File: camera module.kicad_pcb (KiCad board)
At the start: 2 copper layers, 11.4 x 5.7 mm, 152 parts, among them J1 Conn_01x02, J10 Conn_01x04, J11 Conn_01x05, J12 Conn_01x06, J13 Conn_01x02, J15 Conn_02x30_Odd_Even, J17 USB_B_Micro, J18 Conn_01x03, J2 USB_OTG, J3 Conn_01x15, J4 Conn_02x15_Counter_Clockwise, J5 HDMI, J6 Conn_01x15, J7 Conn_01x02, J8 HDMI, J9 HDMI, Q1 EM6K34T2CR, Q10 DMG2305UX, Q11 DMMT5401-7-F, Q12 DMG2305UX, Q2 Q_NMOS_GSD, Q3 Q_NMOS_GSD, Q4 Q_NMOS_GSD, Q5 Q_NMOS_GSD, Q6 Q_NMOS_GSD, Q7 DMMT5401-7-F, Q8 DMG2305UX, Q9 DMMT5401-7-F, SW1 SW_SPST, U1 TPS563208, U10 FSUSB42UMX, U11 USB_A, U2 PAM2306AYPKE, U3 LTC3406ES5-1.2, U4 TS3DDR3812RUAR, U5 TLV70228_SOT23-5, U6 XC6222B181MR-G, U7 LSM6DS3, U8 HDMIULC6-4SC6, U9 AP2331W, Y1 SIT8008AI-73-XXS-33.333333E

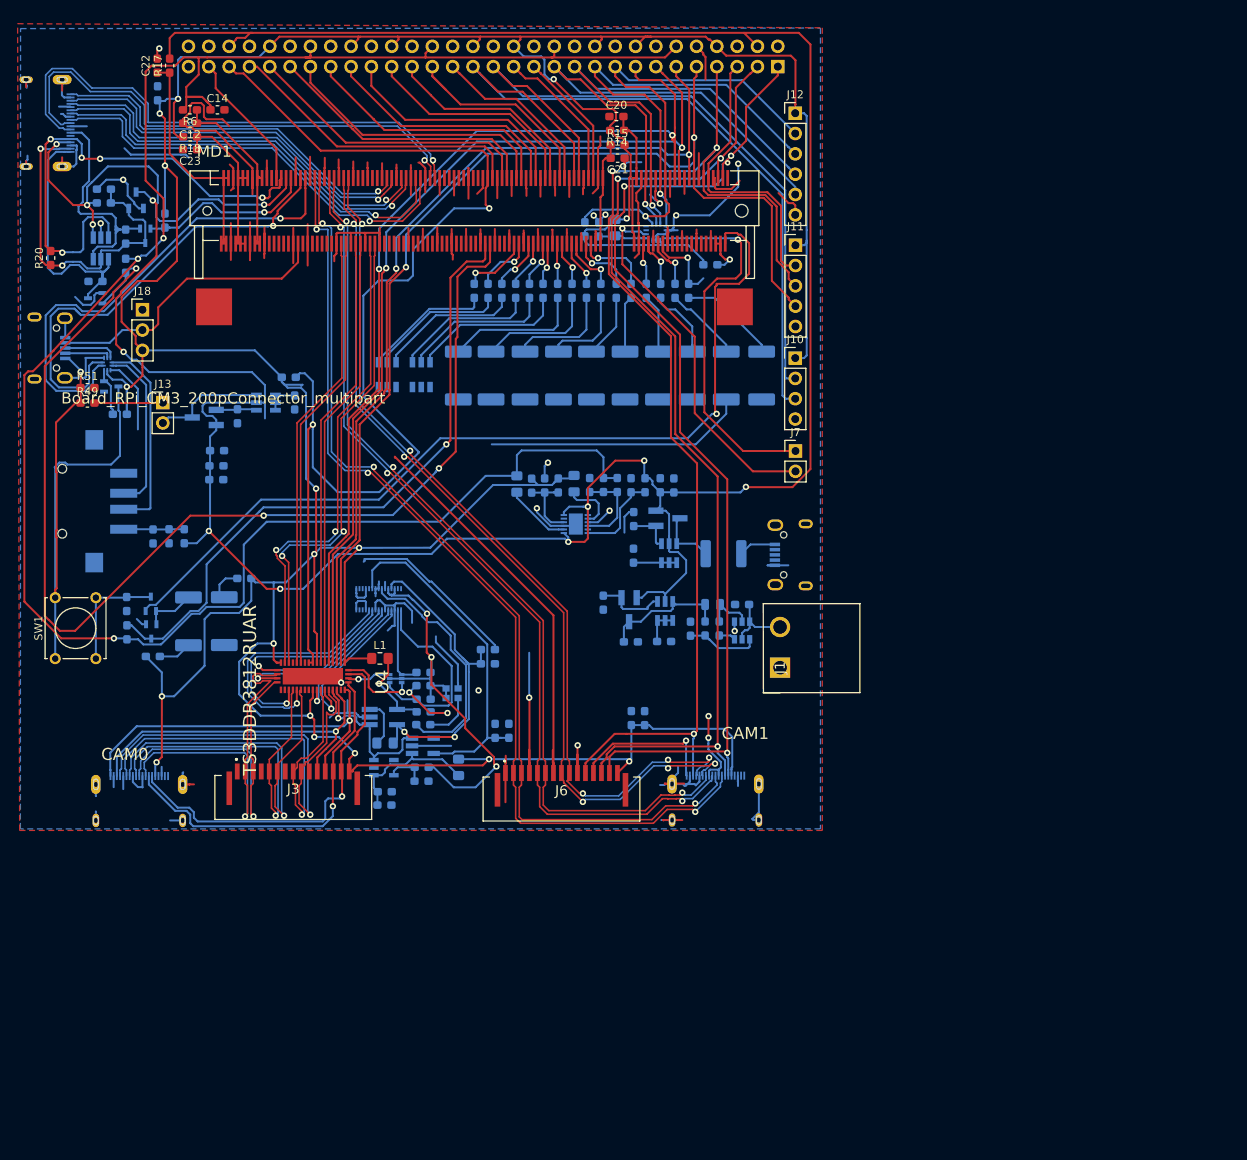
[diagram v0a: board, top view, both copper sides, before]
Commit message: Tweaks to routing, 4th mounting hole added, DRC issues fixed
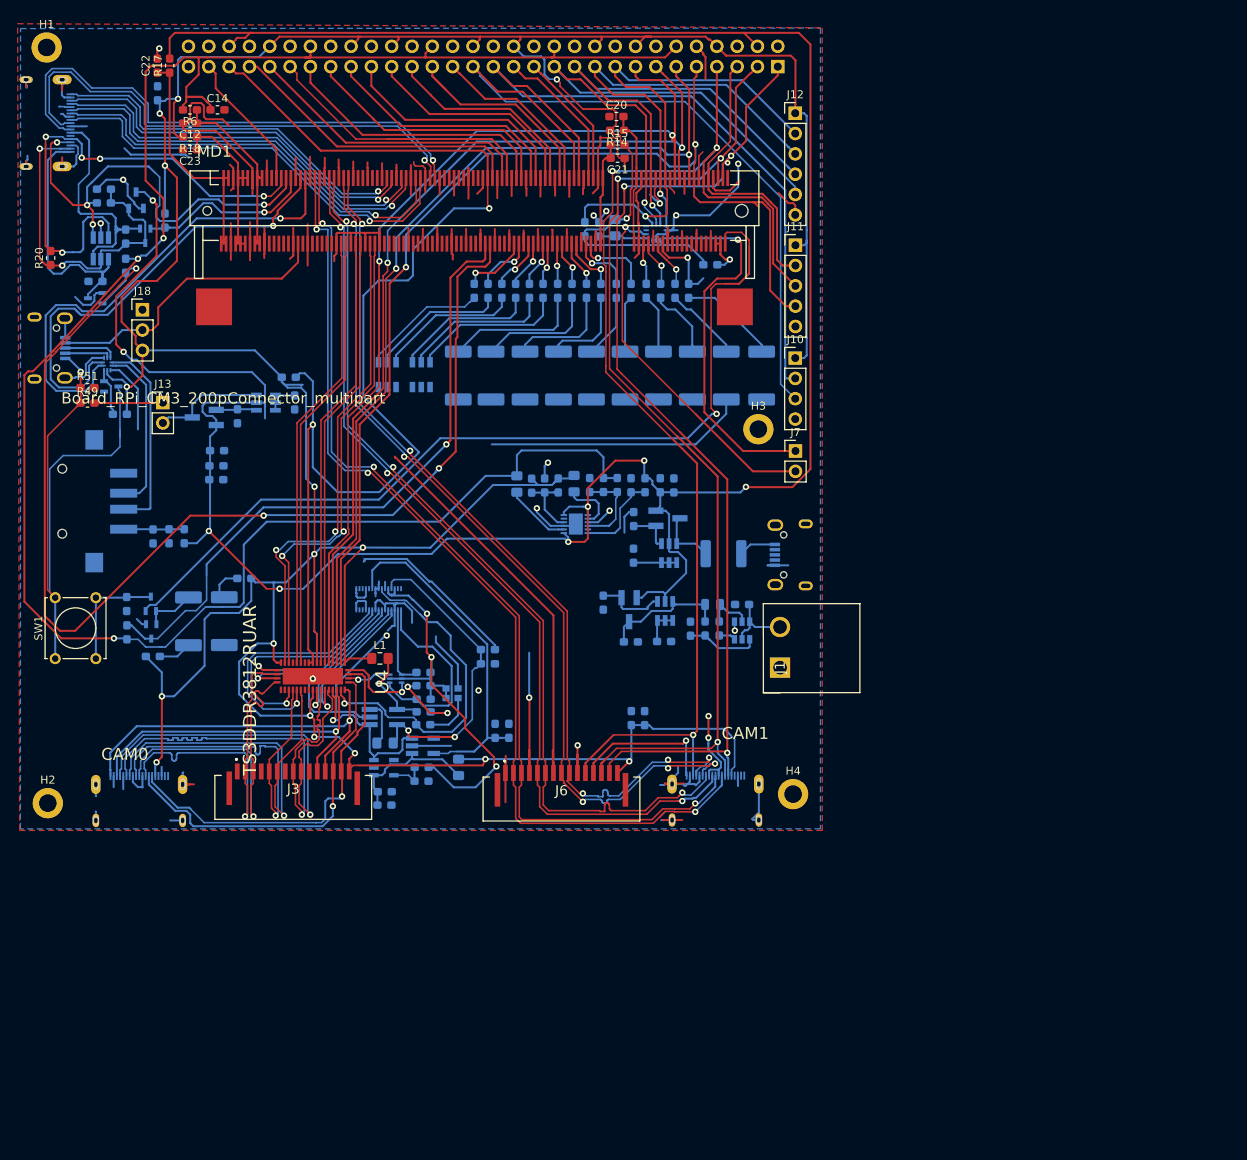
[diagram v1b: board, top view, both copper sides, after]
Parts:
- added H1: MountingHole, MountingHole:MountingHole_2.2mm_M2_DIN965_Pad, F.Cu at (50.9, 38.5)
- added H2: MountingHole, MountingHole:MountingHole_2.2mm_M2_DIN965_Pad, F.Cu at (51.0, 133.0)
- added H3: MountingHole, MountingHole:MountingHole_2.2mm_M2_DIN965_Pad, F.Cu at (139.8, 86.2)
- added H4: MountingHole, MountingHole:MountingHole_2.2mm_M2_DIN965_Pad, F.Cu at (144.2, 131.9)
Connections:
- J4 pad 24: CAM0_CLK -> CAM0_onboard_CLK
- R13 pad 1: CAM0_CLK -> CAM0_onboard_CLK
- U4 pad 37: CAM0_onboard_CK -> CAM0_onboard_CLK
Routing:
- net CAM0_onboard_CLK: track 0.00 -> 44.7 mm, vias 0 -> 1
- net CAM0_CLK: track 29.8 -> 0.00 mm
- net GND: track 567.6 -> 585.4 mm
- net CAM0_offboard_CN: track 53.3 -> 56.5 mm
- net CAM0_offboard_DP0: track 43.2 -> 46.1 mm
- net CD1_SCL: track 127.7 -> 130.5 mm
- net 1V8: track 258.9 -> 261.5 mm
- net 1V2: track 41.1 -> 38.8 mm
- net 3V3: track 535.9 -> 538.0 mm
- net CAM0_onboard_IO0: track 19.8 -> 21.8 mm
- net SPI0_MOSI: track 59.4 -> 61.4 mm
- net CAM0_offboard_DN0: track 47.9 -> 46.1 mm
- net CAM0_offboard_DN1: track 46.6 -> 48.3 mm
- net CAM1_DP1: track 113.0 -> 114.7 mm
- net CAM1_IO0: track 148.2 -> 149.8 mm
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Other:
- net class Default: clearance 0.1 -> 0.125; trace_width 0.25 -> 0.2
- rule trace_clearance: 0.1 -> 0.125
- rule trace_min: 0 -> 0.125
- rule via_min_size: 0.4 -> 0.2

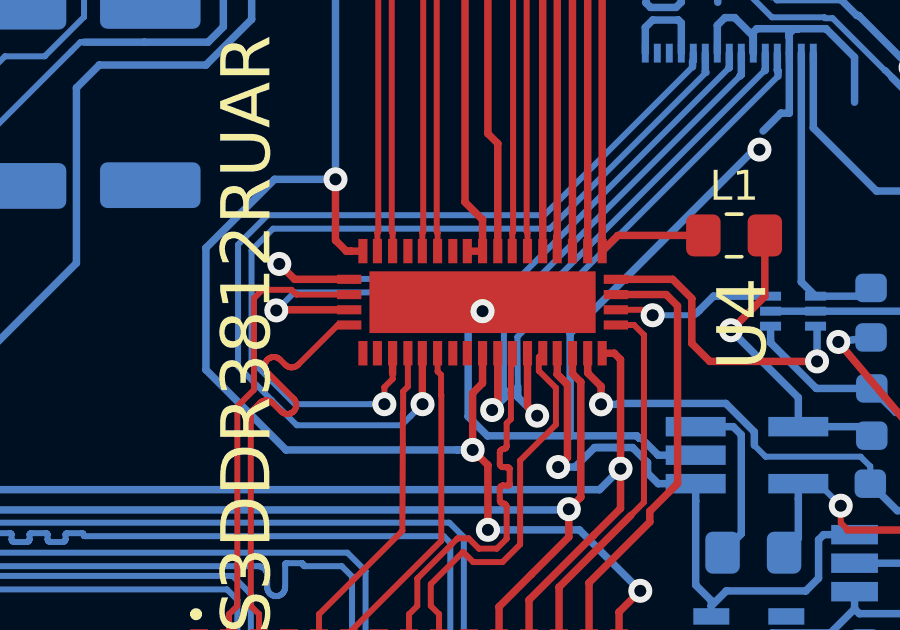
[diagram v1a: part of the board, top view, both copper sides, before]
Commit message: Via for GND on mux moved, ready for checking
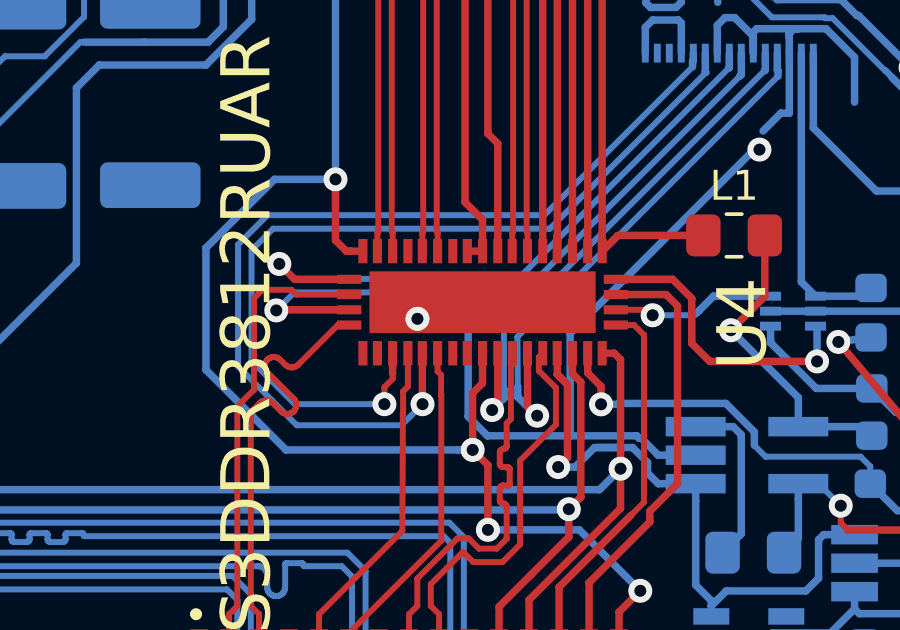
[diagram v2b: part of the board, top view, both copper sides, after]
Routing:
- net GND: track 585.4 -> 586.8 mm
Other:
- rule trace_min: 0.125 -> 0
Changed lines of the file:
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@@
     (thickness 1.6)
     (drawings 42)
-    (tracks 3488)
+    (tracks 3490)
     (zones 0)
     (modules 156)
@@
     (zone_clearance 0.508)
     (zone_45_only no)
-    (trace_min 0.125)
+    (trace_min 0)
     (segment_width 0.2)
     (edge_width 0.15)
@@
   (segment (start 97.049607 118.3) (end 97.1 118.3) (width 0.25) (layer B.Cu) (net 1))
   (segment (start 96.01 118.45) (end 97.049607 118.3) (width 0.25) (layer B.Cu) (net 1))
-  (segment (start 83.67 117.905) (end 84.15 117.425) (width 0.25) (layer B.Cu) (net 1))
   (segment (start 83.67 120.937998) (end 83.67 117.905) (width 0.25) (layer B.Cu) (net 1))
   (segment (start 84.312002 121.58) (end 83.67 120.937998) (width 0.25) (layer B.Cu) (net 1))
@@
   (segment (start 89.44 121.66) (end 89.370344 121.66) (width 0.25) (layer B.Cu) (net 1))
   (segment (start 89.370344 121.66) (end 89.290344 121.58) (width 0.25) (layer B.Cu) (net 1))
-  (via (at 84.15 117.425) (size 0.8) (drill 0.4) (layers F.Cu B.Cu) (net 1))
   (segment (start 87.07 121.58) (end 87.07 118.17) (width 0.25) (layer B.Cu) (net 1))
   (segment (start 87.07 121.58) (end 84.312002 121.58) (width 0.25) (layer B.Cu) (net 1))
@@
   (segment (start 132.4 54.85) (end 132.4 52.08) (width 0.2) (layer F.Cu) (net 1))
   (segment (start 132.4 52.08) (end 132.9 51.58) (width 0.2) (layer F.Cu) (net 1))
+  (via (at 81.98 117.68) (size 0.8) (drill 0.4) (layers F.Cu B.Cu) (net 1))
+  (segment (start 84.15 117.125) (end 84.15 117.425) (width 0.2) (layer F.Cu) (net 1))
+  (segment (start 83.445 117.68) (end 83.67 117.905) (width 0.25) (layer B.Cu) (net 1))
+  (segment (start 81.98 117.68) (end 83.445 117.68) (width 0.25) (layer B.Cu) (net 1))
   (segment (start 74.534999 37.535001) (end 74.534999 37.465001) (width 0.25) (layer F.Cu) (net 2))
   (segment (start 73.685 38.385) (end 74.534999 37.535001) (width 0.25) (layer F.Cu) (net 2))

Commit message: Final files. As sent to manufacture
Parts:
- C10, C11, C15, C16, C17, C18, C19, C6, C7: value C -> 100n
- C31: value C -> 22u
- C32: value C -> 100nf
- C33: value C -> 47u
- D10, D11, D12, D14, D15, D16, D3, D4, D5, D7, D8, D9: footprint LED_SMD:LED_2512_6332Metric_Pad1.52x3.35mm_HandSolder -> LED_SMD:LED_0805_2012Metric_Pad1.15x1.40mm_HandSolder
- L1, L12, L3, L5: footprint Inductor_SMD:L_0805_2012Metric_Pad1.15x1.40mm_HandSolder -> Inductor_SMD:L_0603_1608Metric_Pad1.05x0.95mm_HandSolder
- L6: value L -> 3.3u; footprint Inductor_SMD:L_0805_2012Metric -> Inductor_SMD_local:SDR0805-3R3ML-footprint
- R11, R13, R52, R55, R56, R58, R7: value R -> 10k
- R53, R57, R59: value R -> 47k
- R54: value R -> 56.2k
- moved C31 7.67 mm to (136.8, 115.8)
- moved C32 7.67 mm to (133.9, 118.8)
- moved R54 7.67 mm to (132.1, 118.8)
- moved U1 7.67 mm to (136.8, 119.0)
- moved R55 7.67 mm to (130.3, 118.8)
- moved D15 1.79 mm to (102.3, 77.7)
- moved D4 1.78 mm to (140.2, 77.8)
- moved D5 1.78 mm to (135.8, 77.8)
- moved D11 1.78 mm to (114.8, 77.8)
- moved D7 1.78 mm to (131.6, 77.8)
- moved D14 1.78 mm to (106.3, 77.8)
- moved D12 1.77 mm to (110.7, 77.8)
- moved D9 1.77 mm to (123.2, 77.8)
- moved D10 1.77 mm to (119.0, 77.8)
- moved D8 1.77 mm to (127.3, 77.8)
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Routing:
- net Net-(C33-Pad1): track 16.2 -> 27.7 mm
- net GND: track 586.8 -> 597.5 mm
- net Net-(C32-Pad1): track 6.26 -> 14.2 mm
- net Net-(C31-Pad1): track 9.03 -> 13.7 mm
- net 1V8: track 261.5 -> 264.3 mm
- net Net-(C25-Pad2): track 6.07 -> 8.25 mm
- net Net-(D16-Pad2): track 4.15 -> 6.12 mm
- net Net-(D3-Pad2): track 4.38 -> 5.77 mm
- net EMMC_EN_N_1V8: track 81.6 -> 82.9 mm
- net Net-(D16-Pad1): track 6.42 -> 5.83 mm
- net 5V: track 341.5 -> 341.0 mm
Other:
- net class Default: trace_width 0.2 -> 0.25
